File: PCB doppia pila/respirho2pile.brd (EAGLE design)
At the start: 40.1 x 25.1 mm, 29 parts, among them U1 ICM-20948, U2 1.8V/100mA, X2 32.768kHz

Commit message: Routing completo versione con 2 pile
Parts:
- removed C10: 10uF, GRM188R61A106KE69J:CAPC1608X95N
- removed R5: 330, rcl:R0603
- removed S1: JS102011SAQN, JS102011SAQN:SW_JS102011SAQN
- removed U$1: KSS231GLFS, KSS231GLFS:KSS231GLFS
- removed X2: 32.768kHz, Nordic_nRF:XTAL_3215_N
- added C6: 10u, rcl:C2012
- added R3: 330, rcl:R0603
- added SW1: EG1213, Slide_switch:SW_EG1213
- added SW2: KSS231GLFS, KSS231GLFS:KSS231GLFS
- added X1: 32.768kHz, Nordic_nRF:XTAL_3215_N
- C4, C5: device rcl:C0402 -> rcl:C0603
- R1: value 850k -> 866k
- R2: value 800k -> 806k
- U2: value 1.8V/100mA -> AP2127K-1.8V; device SparkFun-IC-Power:SC70 -> TPS7A05:SOT23-5
- moved 1.8V_TP 25.5 mm to (38.4, 10.4), flipped to the top
- moved L3 24.3 mm to (36.8, 9.91), turned to 270 degrees
- moved J1 23.1 mm to (23.1, 21.1), turned to 0 degrees
- moved L2 22.6 mm to (36.3, 11.4), turned to 180 degrees
- moved C3 22.5 mm to (36.6, 13.7), turned to 270 degrees
- moved C9 21.5 mm to (35.3, 9.14), turned to 90 degrees
- moved C2 21.4 mm to (35.1, 13.5), turned to 270 degrees
- moved C11 20.6 mm to (32.8, 17.0), turned to 0 degrees
- moved C4 18.6 mm to (16.5, 20.1), flipped to the top
- moved C12 17.1 mm to (30.7, 17.0), turned to 180 degrees
- moved R2 16.7 mm to (36.3, 17.5), flipped to the top
- moved C15 15.8 mm to (17.0, 10.7), flipped to the top, turned to 0 degrees
- moved BT1 14.7 mm to (19.8, 12.7), flipped to the bottom, turned to 90 degrees
- moved C5 13.8 mm to (19.8, 17.0), flipped to the top, turned to 270 degrees
- moved C1 13.8 mm to (28.4, 18.3), flipped to the top, turned to 90 degrees
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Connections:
- net GND: now also C4.1, C5.1, C6.1, SW2.P$1; no longer C10.1, C4.2, C5.2, U$1.P$1
- net N$1: now also R3.1; no longer R5.1
- net N$5: now also R3.2; no longer R5.2
- net N$8: now also C4.2, SW1.3; no longer C4.1, S1.3
- net P0.00/XL1: now also X1.1; no longer X2.1
- net P0.01/XL2: now also X1.2; no longer X2.2
- net P06: now also SW2.P$2; no longer U$1.P$2
- net SCL: now also MDBT42Q1.27; no longer MDBT42Q1.26
- net SDA: now also MDBT42Q1.26; no longer MDBT42Q1.27
- net V+BATT: now also SW1.2; no longer S1.2
- net VDD: now also C5.2, C6.2; no longer C10.2, C5.1
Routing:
- net GND: track 211.4 -> 174.2 mm, vias 5 -> 32
- net N$6: track 46.4 -> 19.6 mm, vias 1 -> 0
- net VDD: track 73.7 -> 57.2 mm, vias 1 -> 0
- net N$1: track 2.94 -> 18.7 mm, vias 0 -> 2
- net V+BATT: track 31.0 -> 20.3 mm, vias 1 -> 0
- net P06: track 10.9 -> 18.6 mm, vias 0 -> 1
- net N$9: track 10.8 -> 18.0 mm, vias 1 -> 2
- net N$8: track 20.0 -> 12.8 mm, vias 1 -> 0
- net SWDIO: track 21.8 -> 19.0 mm, vias 0 -> 2
- net N$4: track 3.13 -> 4.98 mm
- net N$5: track 4.34 -> 2.80 mm
- net SDA: track 3.23 -> 1.80 mm, vias 1 -> 0
- net SCL: track 3.15 -> 1.78 mm, vias 1 -> 0
- net N$2: track 1.65 -> 2.88 mm
- net SWDCLK: track 19.6 -> 20.8 mm, vias 0 -> 3
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- added copper zone on layer 1, net GND
- added copper zone on layer 16, net GND
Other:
- board size 40.1 x 25.1 mm -> 24.9 x 26.7 mm
- board text added: "C"
- board text added: "D"
- board text added: "GND"
- board text added: "Vref"

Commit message: Aggiunta bom(da completare)
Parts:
- moved C5 0.78 mm to (20.6, 16.9), turned to 180 degrees
- moved C4 0.57 mm to (17.0, 19.8)
- moved U2 0.51 mm to (17.5, 16.0)
- moved R3 0.36 mm to (20.6, 14.8)
- moved C14 0.10 mm to (19.1, 8.79)
- moved C2 0.07 mm to (35.0, 13.5)
- moved C11 0.05 mm to (32.8, 17.0)
- moved C12 0.05 mm to (30.7, 17.0)
- moved L3 0.05 mm to (36.8, 9.86)
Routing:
- net N$1: track 18.7 -> 23.2 mm
- net N$8: track 12.8 -> 14.6 mm
- net GND: track 174.2 -> 175.8 mm
- net N$6: track 19.6 -> 20.2 mm
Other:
- board text added: "RespirHo'"

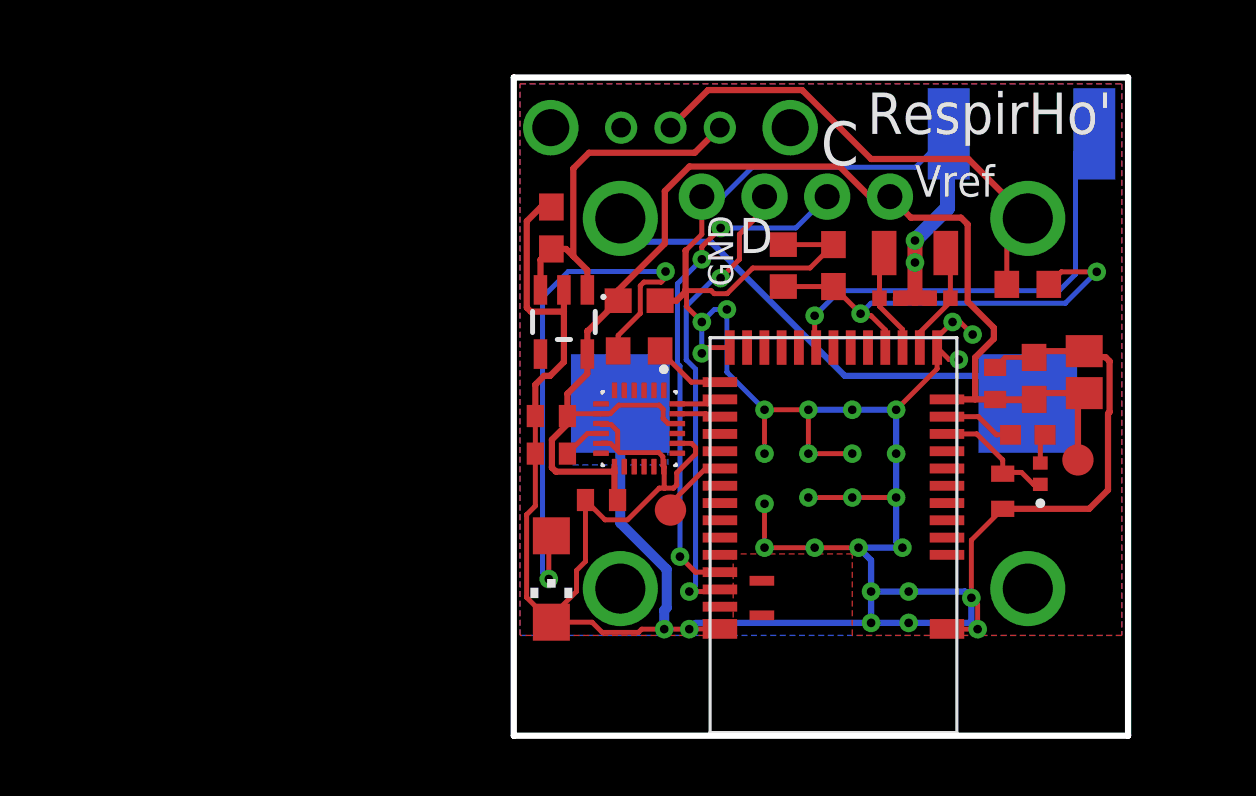
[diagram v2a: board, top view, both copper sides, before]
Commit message: Cambiate delle footprint (R1,R2,R3) e altri piccoli miglioramenti
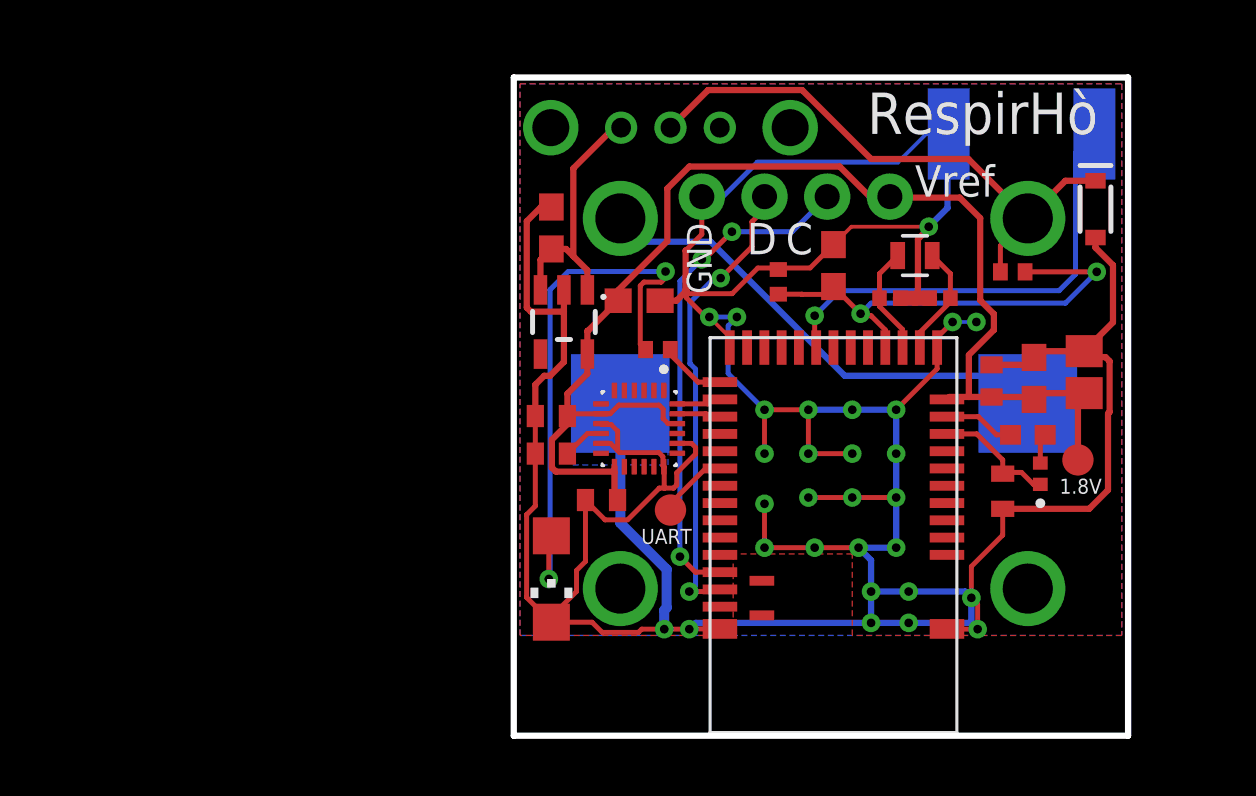
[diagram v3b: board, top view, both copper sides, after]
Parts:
- added D1: 0.5A/40V/420mV, SparkFun-DiscreteSemi:SOD-323
- C2: value 100n -> 100nF; device rcl:C0402 -> CC0402KRX7R6BB104:CAPC1005X60
- R1, R2, R3: device rcl:R0603 -> rcl:R0402
- X1: value 32.768kHz -> (none); device Nordic_nRF:XTAL_3215_N -> XTAL:XTAL_3215_N
- moved R2 0.79 mm to (35.7, 18.0)
- moved R3 0.76 mm to (21.3, 14.9)
- moved R1 0.69 mm to (26.2, 17.6)
- moved C2 0.18 mm to (34.8, 13.6), turned to 90 degrees
- moved X1 0.10 mm to (31.8, 18.7), turned to 0 degrees
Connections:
- net GND: now also C2.2, D1.A; no longer C2.1
- net N$8: now also SW1.1; no longer SW1.3
- net P0.00/XL1: now also X1.2; no longer X1.1
- net P0.01/XL2: now also X1.1; no longer X1.2
- net V+BATT: now also D1.C
- net VDD: now also C2.1; no longer C2.2
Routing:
- net GND: track 175.8 -> 181.9 mm, vias 32 -> 29
- net V+BATT: track 20.3 -> 24.5 mm
- net N$8: track 14.6 -> 10.6 mm
- net VDD: track 57.2 -> 54.0 mm
- net N$9: track 18.0 -> 19.1 mm
- net N$1: track 23.2 -> 22.6 mm
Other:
- board text added: "1.8V"
- board text added: "RespirHò"
- board text added: "UART"
- board text removed: "RespirHo'"

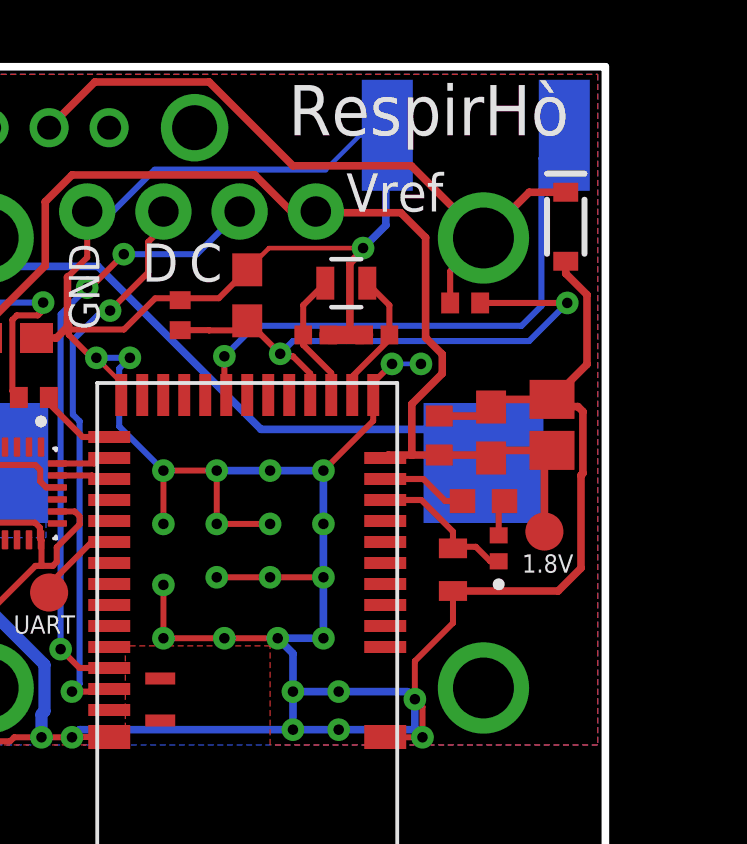
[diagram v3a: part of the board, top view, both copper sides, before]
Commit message: Cambiate altre footprint e componenti non disponibili
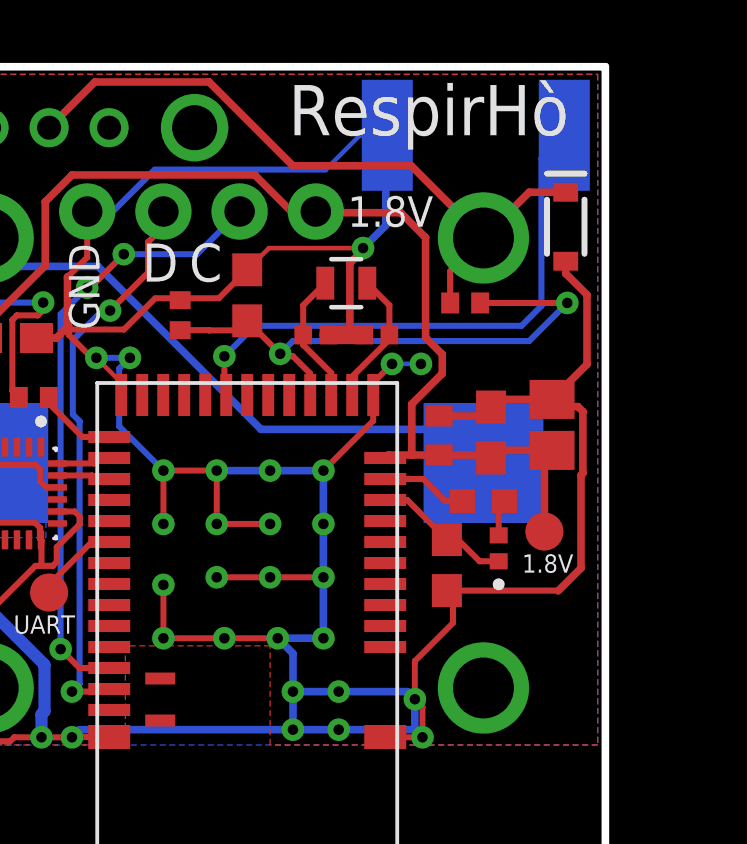
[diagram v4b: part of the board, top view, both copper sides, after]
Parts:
- C9: value 1uF -> 1u; device CC0603KRX7R7BB105:CAPC1608X90N -> rcl:C0603
- J1: value (none) -> HEADERLESS
- LED1: value (none) -> RED
- X1: value (none) -> 32,768kHz
- moved C9 0.25 mm to (35.1, 9.30)
- renumbered C13 to C7, C14 to C8, C15 to C10, L3 to L1
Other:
- board text removed: "Vref"

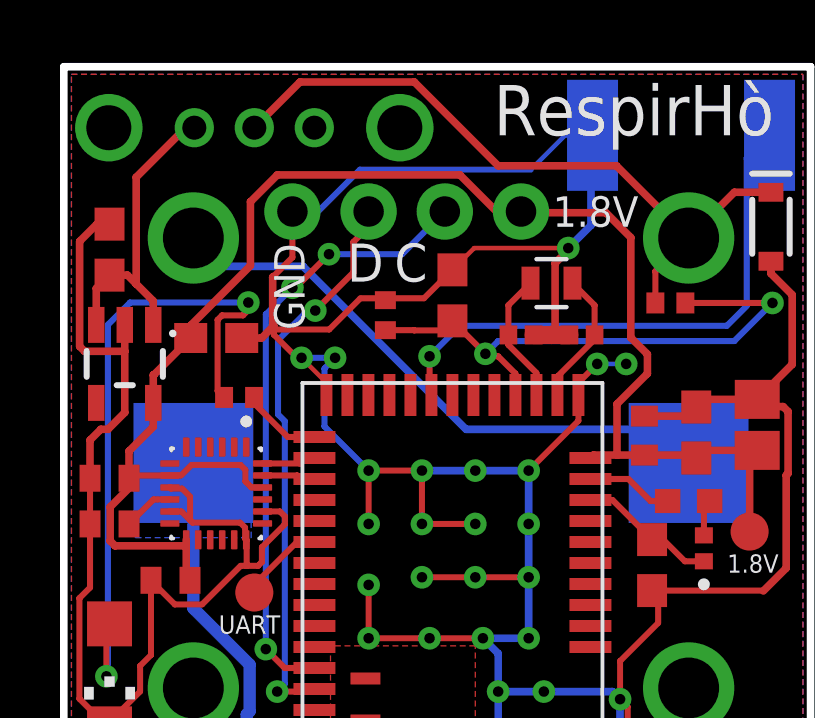
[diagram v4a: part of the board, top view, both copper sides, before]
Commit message: Aggiunte immagini 3d
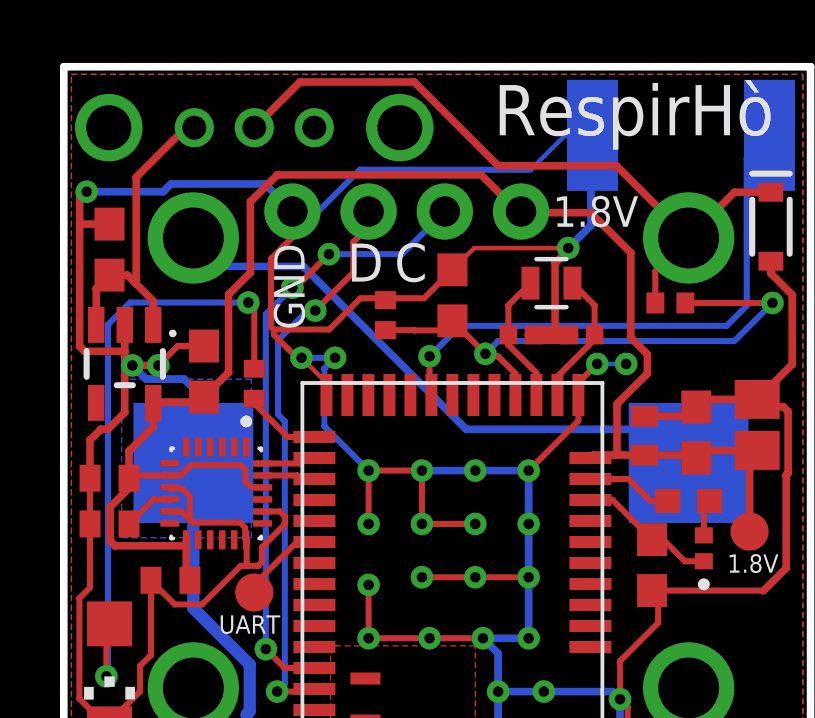
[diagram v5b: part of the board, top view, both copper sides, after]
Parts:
- moved C5 1.19 mm to (20.2, 15.7), turned to 270 degrees
- moved R3 0.68 mm to (21.8, 15.3), turned to 270 degrees
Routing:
- net GND: track 182.2 -> 197.7 mm, vias 29 -> 32
- net N$1: track 22.6 -> 20.8 mm
- net VDD: track 54.0 -> 54.6 mm

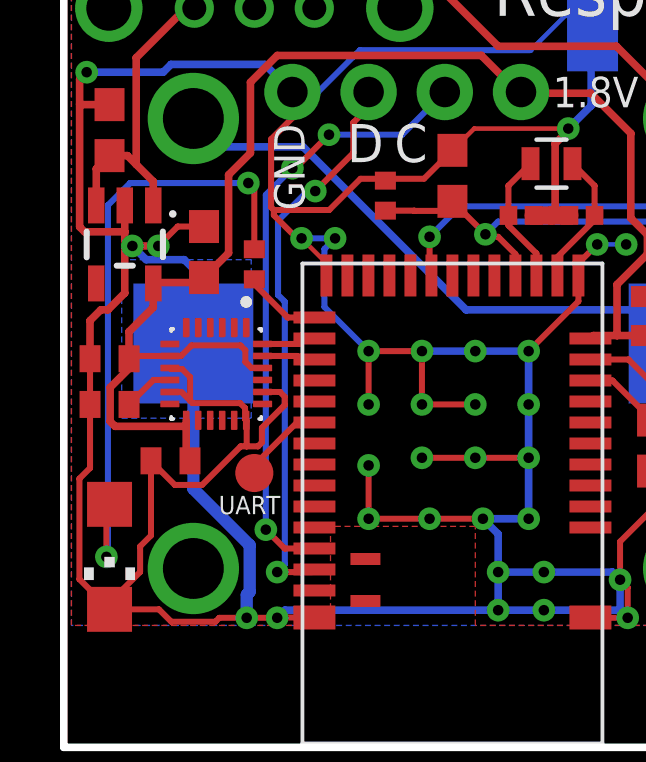
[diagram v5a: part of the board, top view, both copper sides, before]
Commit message: aggiunte resistenze di pull up i2c
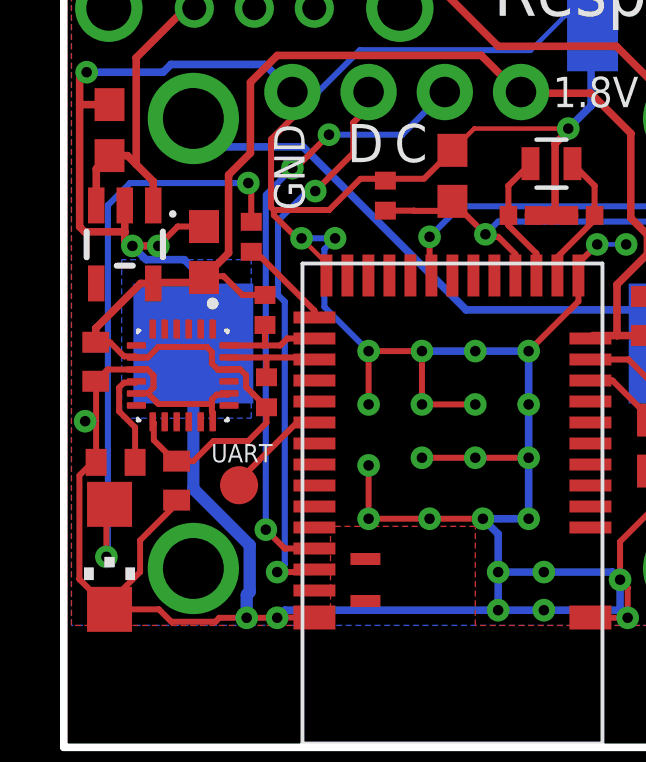
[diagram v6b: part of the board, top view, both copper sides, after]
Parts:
- added R4, R5: 10k, rcl:R0402
- moved C10 1.94 mm to (17.2, 8.74)
- moved U1 1.12 mm to (19.5, 11.6)
- moved R3 0.92 mm to (21.7, 16.3)
- moved C8 0.69 mm to (19.3, 8.13), turned to 90 degrees
- moved UART_TP 0.65 mm to (21.3, 7.98)
- moved C7 0.47 mm to (16.6, 12.1), turned to 90 degrees
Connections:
- net SCL: now also R4.1
- net SDA: now also R5.1
- net VDD: now also R4.2, R5.2
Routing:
- net GND: track 197.7 -> 186.2 mm, vias 32 -> 33
- net VDD: track 54.6 -> 57.5 mm
- net SDA: track 1.80 -> 3.65 mm
- net SCL: track 1.78 -> 3.53 mm
- net N$7: track 1.70 -> 3.37 mm
- net N$1: track 20.8 -> 19.9 mm
- net P0.16: track 2.86 -> 3.47 mm
- net N$5: track 2.63 -> 3.15 mm
